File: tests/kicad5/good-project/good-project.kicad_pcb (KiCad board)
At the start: 2 copper layers, 4 parts, among them P1 CONN_01X02

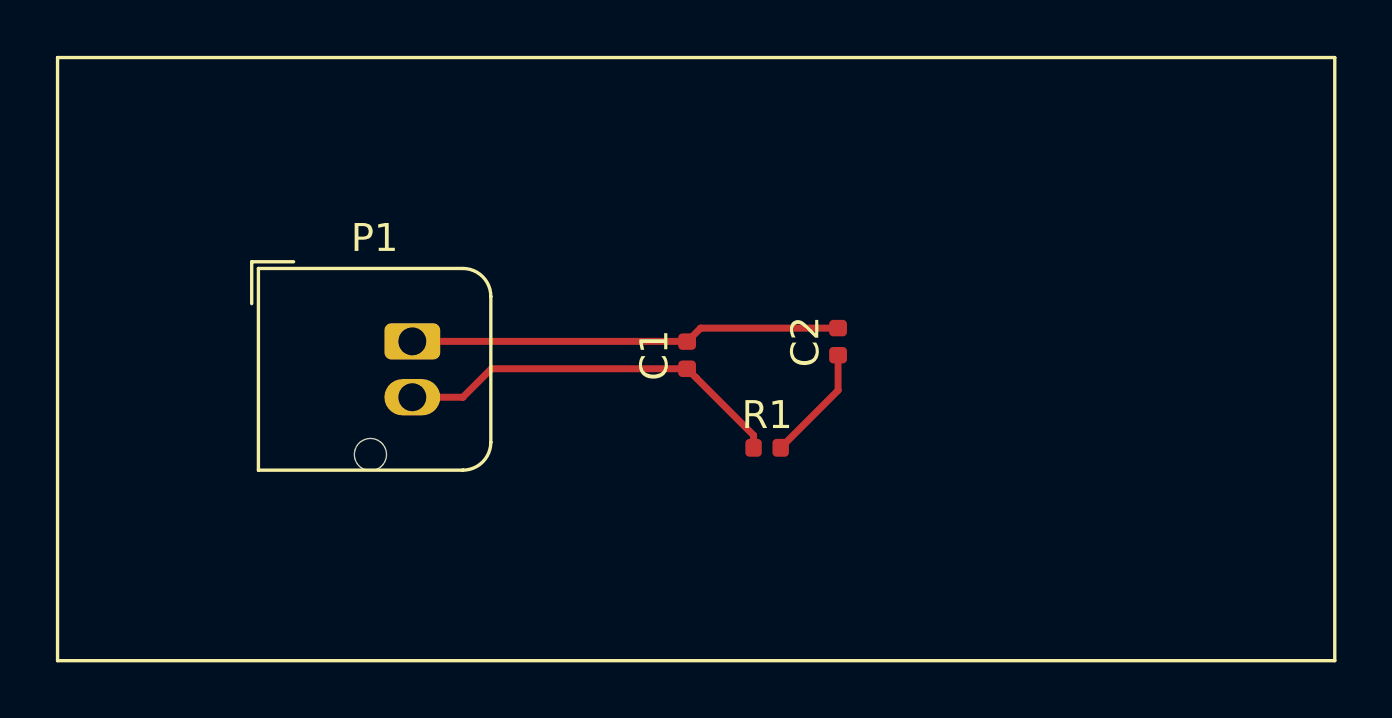
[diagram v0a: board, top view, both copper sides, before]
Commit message: Added 4 layers and comments in Dwgs and Cmts to the "good" test
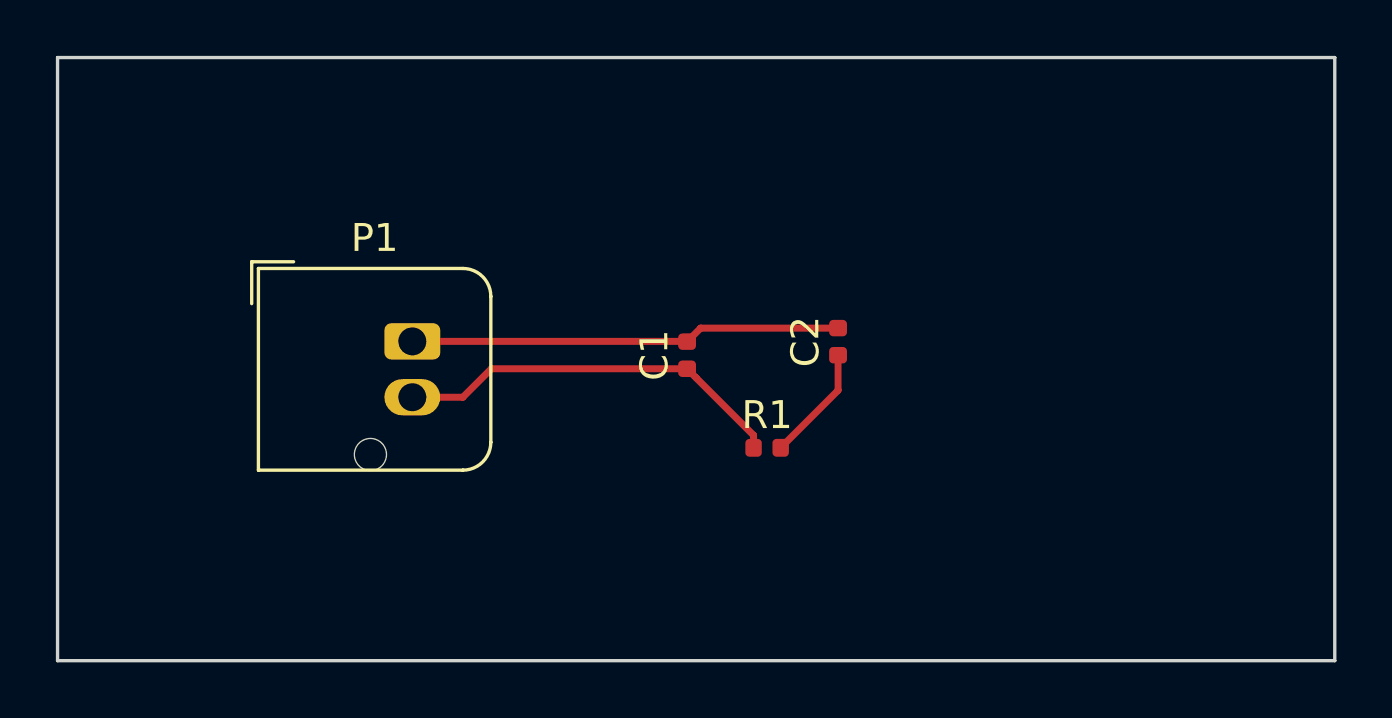
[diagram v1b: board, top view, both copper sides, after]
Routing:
- net (no net): track 0.00 -> 132.0 mm
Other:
- board outline added: 45.7 x 21.6 mm
- copper layers 2 -> 6
- board text added: "Text in Cmts.User"
- board text added: "Text in Dwgs.User"
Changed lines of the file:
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@@
-(kicad_pcb (version 20171130) (host pcbnew 5.1.0)
+(kicad_pcb (version 20171130) (host pcbnew 5.1.5+dfsg1-2~bpo10+1)
   (general
     (thickness 1.6)
-    (drawings 4)
-    (tracks 12)
+    (drawings 6)
+    (tracks 20)
     (zones 0)
     (modules 4)
@@
   (layers
     (0 F.Cu signal)
+    (1 GND.Cu signal)
+    (2 Signal1.Cu signal)
+    (3 Signal2.Cu signal)
+    (4 Power.Cu signal)
     (31 B.Cu signal)
     (32 B.Adhes user)
@@
     )
   )
-  (gr_line (start 187.96 69.85) (end 142.24 69.85) (layer F.SilkS) (width 0.12))
-  (gr_line (start 187.96 91.44) (end 187.96 69.85) (layer F.SilkS) (width 0.12))
-  (gr_line (start 142.24 91.44) (end 187.96 91.44) (layer F.SilkS) (width 0.12))
-  (gr_line (start 142.24 69.85) (end 142.24 91.44) (layer F.SilkS) (width 0.12))
+  (gr_text "Text in Cmts.User" (at 149 93) (layer Cmts.User)
+    (effects (font (size 1 1) (thickness 0.15)))
+  )
+  (gr_text "Text in Dwgs.User" (at 149 68) (layer Dwgs.User)
+    (effects (font (size 1 1) (thickness 0.15)))
+  )
+  (gr_line (start 187.96 69.85) (end 142.24 69.85) (layer Edge.Cuts) (width 0.12))
+  (gr_line (start 187.96 91.44) (end 187.96 69.85) (layer Edge.Cuts) (width 0.12))
+  (gr_line (start 142.24 91.44) (end 187.96 91.44) (layer Edge.Cuts) (width 0.12))
+  (gr_line (start 142.24 69.85) (end 142.24 91.44) (layer Edge.Cuts) (width 0.12))
+  (segment (start 160 73) (end 180 73) (width 0.25) (layer GND.Cu) (net 0))
+  (segment (start 180 73) (end 180 88) (width 0.25) (layer GND.Cu) (net 0))
+  (segment (start 180 88) (end 160 88) (width 0.25) (layer Signal1.Cu) (net 0))
+  (segment (start 160 88) (end 160 73) (width 0.25) (layer Signal1.Cu) (net 0))
+  (segment (start 161 87) (end 179 87) (width 0.25) (layer Signal2.Cu) (net 0))
+  (segment (start 179 87) (end 179 74) (width 0.25) (layer Signal2.Cu) (net 0))
+  (segment (start 161 74) (end 179 74) (width 0.25) (layer Power.Cu) (net 0))
+  (segment (start 161 74) (end 161 87) (width 0.25) (layer Power.Cu) (net 0))
   (segment (start 167.155 83.37) (end 165.1 81.315) (width 0.25) (layer F.Cu) (net 1))
   (segment (start 167.155 83.82) (end 167.155 83.37) (width 0.25) (layer F.Cu) (net 1))
